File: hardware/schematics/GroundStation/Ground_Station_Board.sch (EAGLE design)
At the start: 11 parts

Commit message: board's smaller now
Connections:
- net +3V3: now also U$2.3V3; no longer U$2.3V3_LO
- net LED_1: now also U$2.24; no longer U$2.37/A18
- net LED_2: now also U$2.25; no longer U$2.38/A19
- net LED_3: now also U$2.26; no longer U$2.39/A20
- net XBEE_EN: now also U$2.3/CANTX; no longer U$2.22/A8
- net XBEE_RST: now also U$2.4/CANRX; no longer U$2.20/A6
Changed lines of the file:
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@@
 <attribute name="VALUE" x="-55.88" y="93.98" size="1.778" layer="96" rot="MR0"/>
 </instance>
-<instance part="+3V2" gate="G$1" x="-129.54" y="106.68" smashed="yes" rot="MR0">
-<attribute name="VALUE" x="-132.08" y="106.68" size="1.778" layer="96" rot="MR0"/>
+<instance part="+3V2" gate="G$1" x="-53.34" y="73.66" smashed="yes" rot="MR0">
+<attribute name="VALUE" x="-45.72" y="73.66" size="1.778" layer="96" rot="MR0"/>
 </instance>
 <instance part="GND4" gate="1" x="-129.54" y="96.52" smashed="yes" rot="MR0">
@@
 </segment>
 <segment>
-<pinref part="U$2" gate="G$1" pin="22/A8"/>
-<wire x1="-111.76" y1="91.44" x2="-121.92" y2="91.44" width="0.1524" layer="91"/>
-<label x="-134.62" y="91.44" size="1.778" layer="95"/>
+<pinref part="U$2" gate="G$1" pin="3/CANTX"/>
+<wire x1="-71.12" y1="91.44" x2="-68.58" y2="91.44" width="0.1524" layer="91"/>
+<wire x1="-68.58" y1="91.44" x2="-68.58" y2="83.82" width="0.1524" layer="91"/>
+<wire x1="-68.58" y1="83.82" x2="-55.88" y2="83.82" width="0.1524" layer="91"/>
+<label x="-55.88" y="83.82" size="1.778" layer="95"/>
 </segment>
 </net>
@@
 </segment>
 <segment>
-<pinref part="U$2" gate="G$1" pin="20/A6"/>
-<wire x1="-111.76" y1="86.36" x2="-121.92" y2="86.36" width="0.1524" layer="91"/>
-<label x="-134.62" y="86.36" size="1.778" layer="95"/>
+<pinref part="U$2" gate="G$1" pin="4/CANRX"/>
+<wire x1="-71.12" y1="88.9" x2="-71.12" y2="81.28" width="0.1524" layer="91"/>
+<wire x1="-71.12" y1="81.28" x2="-55.88" y2="81.28" width="0.1524" layer="91"/>
+<label x="-55.88" y="81.28" size="1.778" layer="95"/>
 </segment>
 </net>
@@
 </net>
 <net name="+3V3" class="0">
-<segment>
-<pinref part="+3V2" gate="G$1" pin="+3V3"/>
-<wire x1="-129.54" y1="101.6" x2="-129.54" y2="104.14" width="0.1524" layer="91"/>
-<wire x1="-129.54" y1="101.6" x2="-116.84" y2="101.6" width="0.1524" layer="91"/>
-<wire x1="-116.84" y1="101.6" x2="-116.84" y2="96.52" width="0.1524" layer="91"/>
-<pinref part="U$2" gate="G$1" pin="3V3_LO"/>
-<wire x1="-116.84" y1="96.52" x2="-111.76" y2="96.52" width="0.1524" layer="91"/>
-</segment>
 <segment>
 <pinref part="XBEE" gate="G$1" pin="VCC"/>
@@
 <junction x="-104.14" y="15.24"/>
 </segment>
+<segment>
+<pinref part="U$2" gate="G$1" pin="3V3"/>
+<pinref part="+3V2" gate="G$1" pin="+3V3"/>
+<wire x1="-71.12" y1="66.04" x2="-53.34" y2="66.04" width="0.1524" layer="91"/>
+<wire x1="-53.34" y1="66.04" x2="-53.34" y2="71.12" width="0.1524" layer="91"/>
+</segment>
 </net>
 <net name="LED_1" class="0">
-<segment>
-<pinref part="U$2" gate="G$1" pin="37/A18"/>
-<wire x1="-111.76" y1="53.34" x2="-121.92" y2="53.34" width="0.1524" layer="91"/>
-<label x="-132.08" y="53.34" size="1.778" layer="95"/>
-</segment>
 <segment>
 <wire x1="-88.9" y1="154.94" x2="-81.28" y2="154.94" width="0.1524" layer="91"/>
@@
 <pinref part="R1" gate="G$1" pin="2"/>
 </segment>
+<segment>
+<pinref part="U$2" gate="G$1" pin="24"/>
+<wire x1="-71.12" y1="63.5" x2="-63.5" y2="63.5" width="0.1524" layer="91"/>
+<label x="-63.5" y="63.5" size="1.778" layer="95"/>
+</segment>
 </net>
 <net name="LED_2" class="0">
-<segment>
-<pinref part="U$2" gate="G$1" pin="38/A19"/>
-<wire x1="-111.76" y1="55.88" x2="-121.92" y2="55.88" width="0.1524" layer="91"/>
-<label x="-132.08" y="55.88" size="1.778" layer="95"/>
-</segment>
 <segment>
 <wire x1="-88.9" y1="149.86" x2="-81.28" y2="149.86" width="0.1524" layer="91"/>
@@
 <pinref part="R2" gate="G$1" pin="2"/>
 </segment>
+<segment>
+<pinref part="U$2" gate="G$1" pin="25"/>
+<wire x1="-71.12" y1="60.96" x2="-63.5" y2="60.96" width="0.1524" layer="91"/>
+<label x="-63.5" y="60.96" size="1.778" layer="95"/>
+</segment>
 </net>
 <net name="LED_3" class="0">
-<segment>
-<pinref part="U$2" gate="G$1" pin="39/A20"/>
-<wire x1="-111.76" y1="58.42" x2="-121.92" y2="58.42" width="0.1524" layer="91"/>
-<label x="-132.08" y="58.42" size="1.778" layer="95"/>
-</segment>
 <segment>
 <wire x1="-88.9" y1="144.78" x2="-81.28" y2="144.78" width="0.1524" layer="91"/>
@@
 <pinref part="R3" gate="G$1" pin="2"/>
 </segment>
-</net>
+<segment>
+<pinref part="U$2" gate="G$1" pin="26"/>
+<wire x1="-71.12" y1="58.42" x2="-63.5" y2="58.42" width="0.1524" layer="91"/>
+<label x="-63.5" y="58.42" size="1.778" layer="95"/>
+</segment>
+</net>

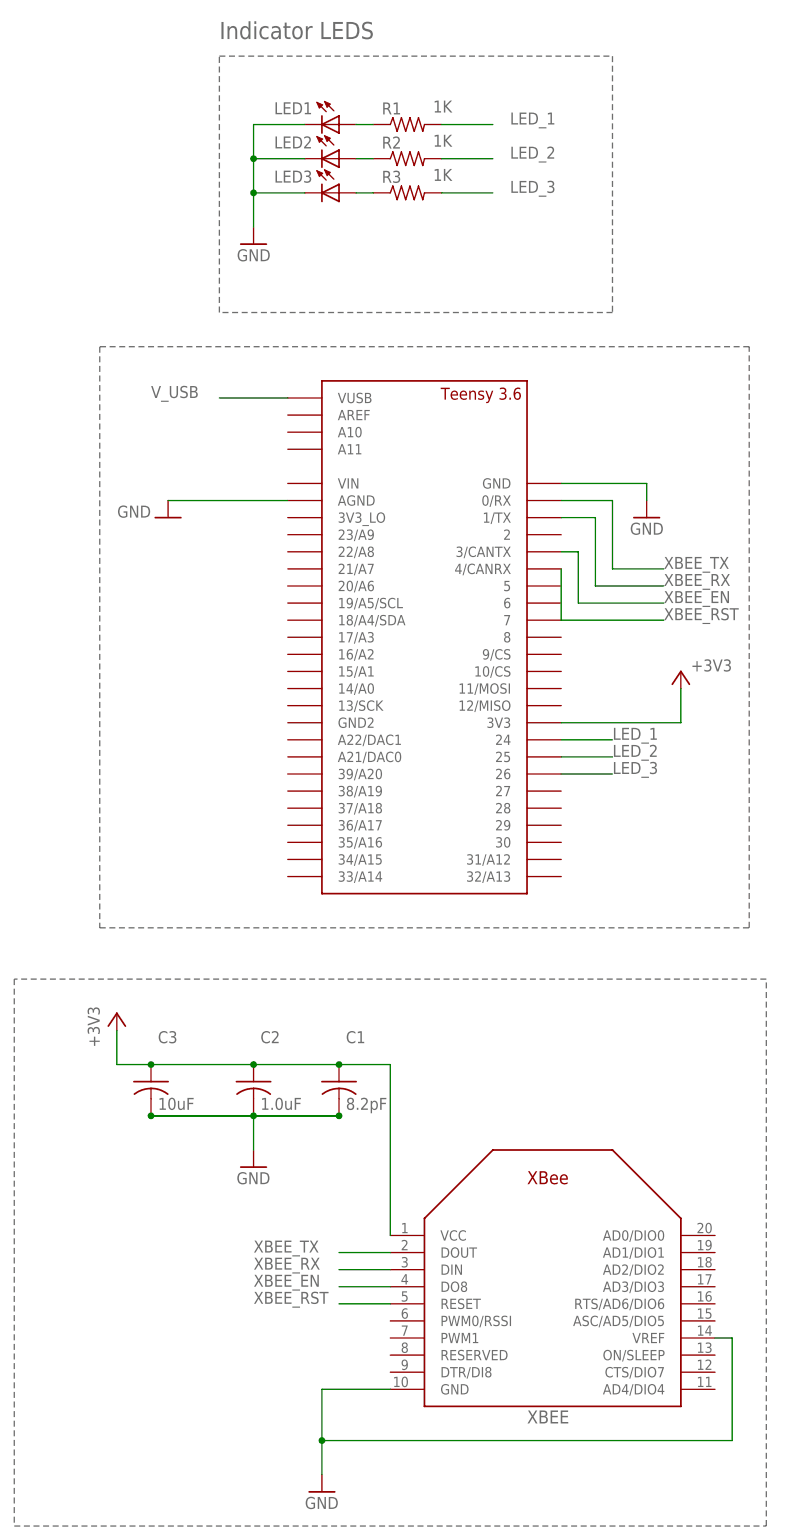
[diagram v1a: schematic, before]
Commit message: Changed Xbee -> Xbee-Pro | Added render png
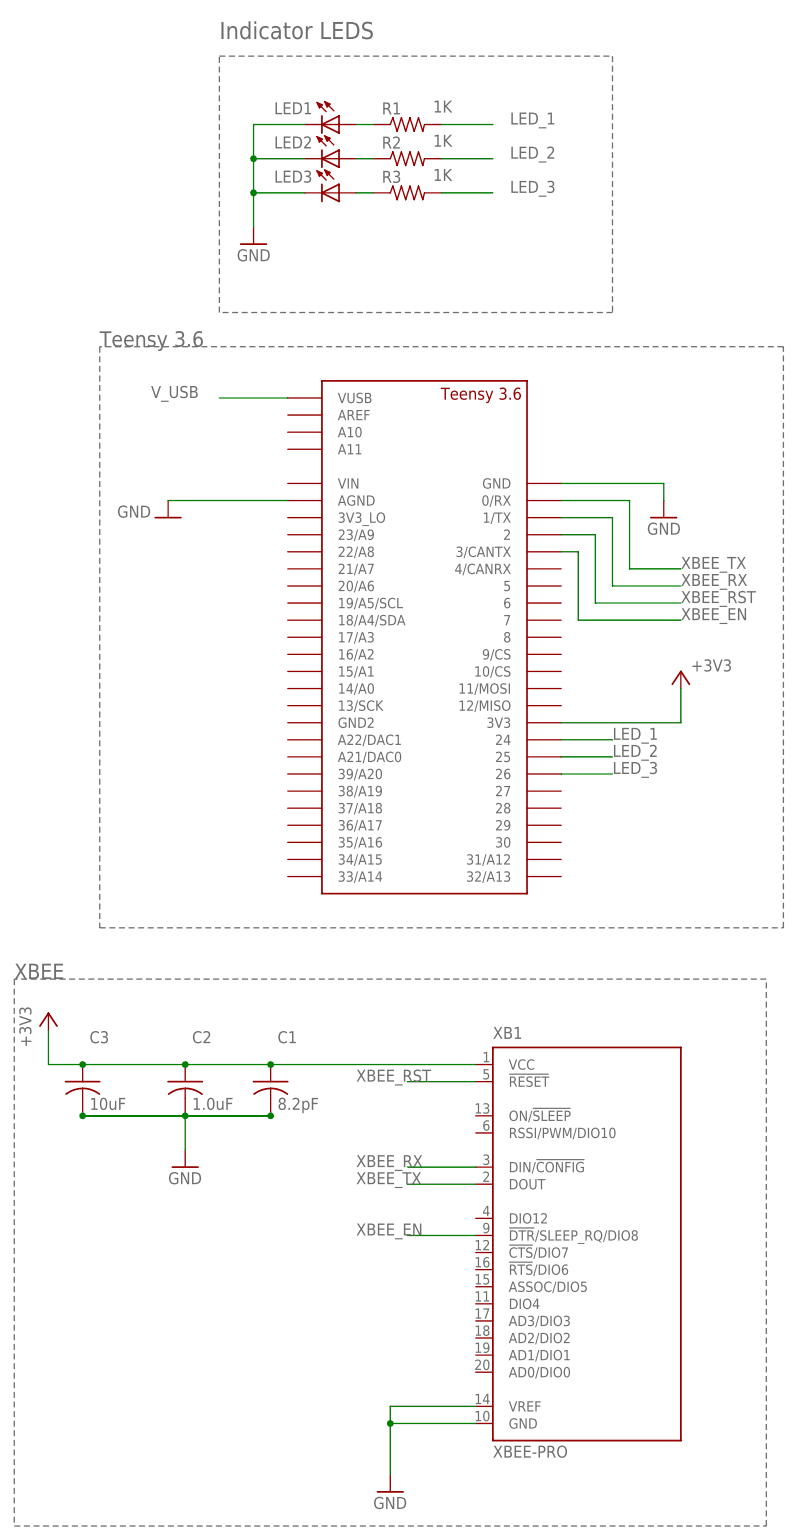
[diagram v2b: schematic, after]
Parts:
- removed XBEE: XBEE, adafruit:XBEE
- added XB1: XBEE-PRO, xbee:XBEE-PRO
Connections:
- net +3V3: now also XB1.VCC; no longer XBEE.VCC
- net GND: now also XB1.GND, XB1.VREF; no longer XBEE.GND, XBEE.VREF
- net XBEE_EN: now also XB1.!DTR!/SLEEP_RQ/DIO8; no longer XBEE.DO8
- net XBEE_RST: now also U$2.2, XB1.!RESET; no longer U$2.4/CANRX, XBEE.RESET
- net XBEE_RX: now also XB1.DIN/!CONFIG; no longer XBEE.DIN
- net XBEE_TX: now also XB1.DOUT; no longer XBEE.DOUT
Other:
- note added: "Teensy 3.6"
- note added: "XBEE"
- moved on the sheet: C1, C2, C3
